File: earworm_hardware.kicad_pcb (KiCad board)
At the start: 2 copper layers, 37 parts, among them J1 Conn_01x02, J2 Conn_01x05, T1 LPR6235-752SMRC, U1 LTC3108EDE-TRPBF, U2 ADXL367BCCZ-RL7, U3 nRF54L15-QFXX, X1 32MHz

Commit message: Initial PCB Layout
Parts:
- removed the C11 at (83.0, 82.1)
- added C4: 10uF, Capacitor_SMD:C_0603_1608Metric, F.Cu at (93.6, 76.5)
- added X1: 32.768 kHz, earworm:Crystal_SMD_ECS_2012-2Pin_2.0x1.2mm, F.Cu at (94.1, 80.5)
- C1: renamed from C10; footprint Capacitor_SMD:C_0603_1608Metric -> Capacitor_SMD:C_0402_1005Metric
- C10: renamed from C7; footprint Capacitor_SMD:C_0603_1608Metric_Pad1.08x0.95mm_HandSolder -> Capacitor_SMD:C_0402_1005Metric; moved to B.Cu
- C11: renamed from C9; footprint Capacitor_SMD:C_0603_1608Metric -> Capacitor_SMD:C_0402_1005Metric; moved to B.Cu
- C12: renamed from C15; footprint Capacitor_SMD:C_0603_1608Metric -> Capacitor_SMD:C_0402_1005Metric
- C13: renamed from C8; footprint Capacitor_SMD:C_0603_1608Metric -> Capacitor_SMD:C_0402_1005Metric; moved to B.Cu
- C14: renamed from C16; footprint Capacitor_SMD:C_0603_1608Metric -> Capacitor_SMD:C_0402_1005Metric
- C15: renamed from C18; footprint Capacitor_SMD:C_0603_1608Metric -> Capacitor_SMD:C_0402_1005Metric
- C16: renamed from C19; footprint Capacitor_SMD:C_0603_1608Metric -> Capacitor_SMD:C_0402_1005Metric
- C17: renamed from C2; footprint Capacitor_SMD:C_0603_1608Metric -> Capacitor_SMD:C_0402_1005Metric
- C19: renamed from C5; moved to B.Cu
- C2: renamed from C12; footprint Capacitor_SMD:C_0603_1608Metric -> Capacitor_SMD:C_0402_1005Metric
- C20: renamed from C3; footprint Capacitor_SMD:C_0603_1608Metric -> Capacitor_SMD:C_0402_1005Metric
- C22: renamed from C4; footprint Capacitor_SMD:C_0603_1608Metric -> Capacitor_SMD:C_0402_1005Metric
- C3: renamed from C14; footprint Capacitor_SMD:C_0603_1608Metric -> Capacitor_SMD:C_0402_1005Metric
- C5: renamed from C13; footprint Capacitor_SMD:C_0603_1608Metric -> Capacitor_SMD:C_0402_1005Metric
- C6: renamed from C17; footprint Capacitor_SMD:C_0603_1608Metric -> Capacitor_SMD:C_0402_1005Metric
- FB1: footprint Inductor_SMD:L_0603_1608Metric -> Inductor_SMD:L_0402_1005Metric; moved to B.Cu
- FB2: footprint Inductor_SMD:L_0603_1608Metric -> Inductor_SMD:L_0402_1005Metric
- R1: renamed from R2; footprint Resistor_SMD:R_0603_1608Metric_Pad0.98x0.95mm_HandSolder -> Resistor_SMD:R_0402_1005Metric
- R2: renamed from R1; footprint Resistor_SMD:R_0603_1608Metric -> Resistor_SMD:R_0402_1005Metric; moved to B.Cu
- U2: moved to B.Cu
- moved C18 32.3 mm to (106.2, 87.5), turned to 180 degrees
- moved T1 30.0 mm to (105.0, 92.4), turned to -90 degrees
- moved C21 26.0 mm to (93.4, 86.9), turned to -90 degrees
- moved R1 21.9 mm to (103.9, 85.0)
- moved J2 21.8 mm to (107.7, 84.7), turned to -90 degrees
- moved U3 21.0 mm to (96.5, 92.7)
- moved C10 19.3 mm to (96.6, 75.7)
- moved C19 18.9 mm to (96.9, 87.2)
- moved C16 18.1 mm to (101.0, 75.6)
- moved C6 17.0 mm to (103.9, 84.0)
- moved L3 16.2 mm to (106.6, 80.7)
- moved C5 16.2 mm to (99.2, 86.7), turned to -90 degrees
- moved C15 16.1 mm to (101.0, 76.6)
- moved X2 15.7 mm to (104.8, 76.6), turned to -90 degrees
- moved C2 15.6 mm to (95.8, 75.6), turned to 90 degrees
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- renumbered C1 to C18, C6 to C21, C20 to C7, C21 to C8, C22 to C9, J2 to J1, J1 to J2, L2 to L1, L3 to L2, L4 to L3, L1 to L4, U3 to U1, U1 to U3, X1 to X2
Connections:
- U1 pad 1: unconnected-(U3-P1.00-Pad1) -> Net-(U1-P1.00)
- U1 pad 2: unconnected-(U3-P1.01-Pad2) -> Net-(U1-P1.01)
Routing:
- net Net-(U1-P2.05): track 0.00 -> 13.3 mm
- net Net-(U1-P2.02): track 0.00 -> 12.5 mm, vias 0 -> 1
- net Net-(U1-P2.01): track 0.00 -> 10.6 mm, vias 0 -> 1
- net Net-(U1-P2.04): track 0.00 -> 9.43 mm
- net Net-(T1-SB): track 0.00 -> 8.52 mm
- net Net-(U1-P2.03): track 0.00 -> 8.35 mm
- net Net-(J2-Pin_1): track 0.00 -> 5.71 mm
- net Net-(T1-AB): track 0.00 -> 5.36 mm
- net /Thermal Energy Harvesting Chain/VSTORE: track 0.00 -> 5.22 mm
- net Net-(U1-~{RESET}): track 0.00 -> 4.74 mm
- net Net-(U1-XC2): track 0.00 -> 4.47 mm
- net Net-(U1-XC1): track 0.00 -> 4.47 mm
- net Net-(U1-P1.01): track 0.00 -> 3.48 mm
- net GND: track 0.00 -> 3.30 mm
- net Net-(U1-DECD): track 0.00 -> 3.11 mm
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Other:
- board outline added: 17.3 x 22.2 mm
- board text added: "EECS 598 EARWORM"

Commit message: Initial RF layout
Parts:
- moved FB2 0.16 mm to (99.3, 74.6)
- moved L3 0.07 mm to (106.7, 80.8)
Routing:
- net Net-(U1-DECA): track 0.00 -> 9.02 mm, vias 0 -> 2
- net Net-(U2-VDDIO): track 0.00 -> 3.20 mm
- net Net-(U1-DECD): track 3.11 -> 5.85 mm
- net GND: track 3.30 -> 5.55 mm, vias 0 -> 1
- net VDD: track 2.39 -> 4.27 mm, vias 0 -> 1
- net Net-(U2-VREG_OUT): track 0.00 -> 1.43 mm
- added copper zone on B.Cu, net GND
- added copper zone on F.Cu, net Net-(U1-DECA)
- added copper zone on B.Cu, net Net-(U2-VS)

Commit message: DRC passed, everything done except RF
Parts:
- J1: footprint Connector_PinHeader_1.00mm:PinHeader_1x05_P1.00mm_Vertical -> Connector_PinHeader_2.54mm:PinHeader_1x05_P2.54mm_Vertical
- J2: footprint Connector_PinHeader_1.00mm:PinHeader_1x02_P1.00mm_Vertical -> Connector_PinHeader_2.54mm:PinHeader_1x02_P2.54mm_Vertical
- moved J1 6.94 mm to (93.6, 97.9), turned to 90 degrees
- moved J2 2.53 mm to (108.8, 87.0), turned to 180 degrees
- moved C18 2.00 mm to (105.9, 85.5), turned to 90 degrees
- moved C6 0.74 mm to (103.7, 84.7)
- moved R1 0.74 mm to (103.7, 85.7)
- moved C17 0.45 mm to (100.0, 92.7)
- moved C22 0.43 mm to (96.7, 89.8)
- moved C12 0.42 mm to (98.7, 76.6)
- moved C2 0.41 mm to (95.7, 76.0)
- moved C20 0.30 mm to (100.0, 91.7)
- moved T1 0.27 mm to (104.8, 92.4)
- moved L4 0.20 mm to (97.0, 75.6)
- moved C1 0.20 mm to (93.9, 82.7)
- moved C19 0.20 mm to (96.9, 87.4)
- moved C15 0.20 mm to (101.0, 76.4)
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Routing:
- net VDD: track 4.27 -> 47.7 mm, vias 1 -> 7
- net /nRF54L15 RFSoC/SWCLK: track 0.00 -> 19.2 mm, vias 0 -> 1
- net /nRF54L15 RFSoC/NRST: track 0.00 -> 16.6 mm, vias 0 -> 1
- net /nRF54L15 RFSoC/SWDIO: track 0.00 -> 16.6 mm, vias 0 -> 1
- net Net-(U1-DECA): track 9.02 -> 18.7 mm
- net GND: track 5.55 -> 14.6 mm, vias 1 -> 39
- net Net-(T1-SB): track 8.52 -> 0.00 mm
- net /Thermal Energy Harvesting Chain/VSTORE: track 5.22 -> 11.5 mm
- net Net-(J2-Pin_1): track 5.71 -> 1.70 mm
- net Net-(U3-VAUX): track 2.07 -> 5.98 mm, vias 0 -> 2
- net Net-(U1-P2.04): track 9.43 -> 13.1 mm, vias 0 -> 1
- net Net-(U1-P2.03): track 8.35 -> 11.2 mm, vias 0 -> 1
- net Net-(U1-P2.05): track 13.3 -> 16.1 mm, vias 0 -> 1
- net Net-(U1-P2.02): track 12.5 -> 11.8 mm
- net Net-(U1-DECD): track 5.85 -> 5.21 mm
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- added copper zone on F.Cu, net GND
- added copper zone on F.Cu, net Net-(J2-Pin_1)
- added copper zone on F.Cu, net Net-(T1-SB)
- added copper zone on F.Cu, net VDD
- removed copper zone on F.Cu, net Net-(U1-DECA)
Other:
- board size 17.3 x 22.2 mm -> 19.1 x 26.3 mm

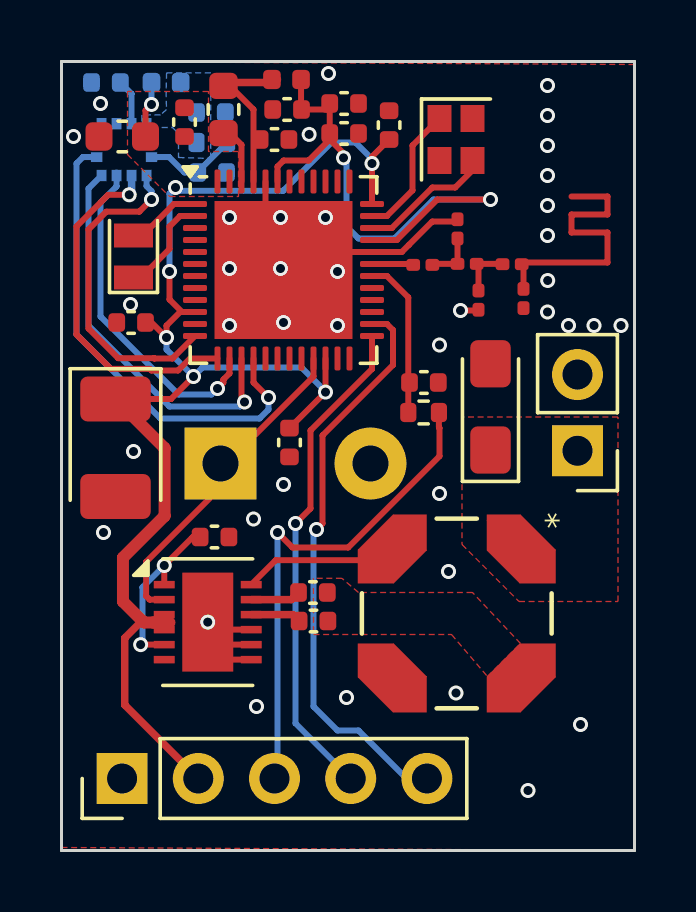
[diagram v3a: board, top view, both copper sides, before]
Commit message: 4 layer version, RF trace impedence matched
Missing SMA connector and a net tie for the other end of the inverted F
antenna to GND.
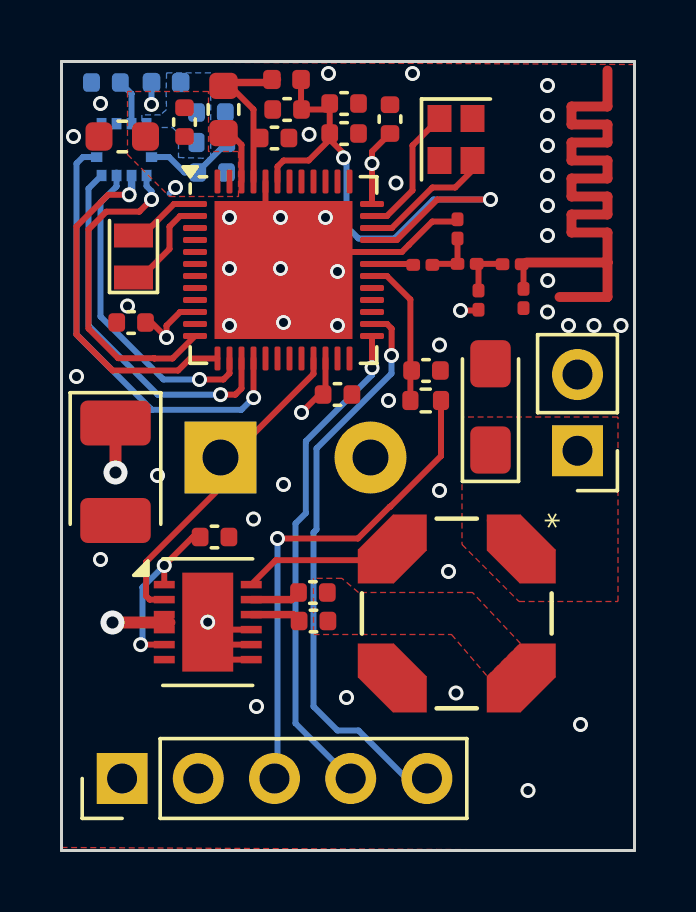
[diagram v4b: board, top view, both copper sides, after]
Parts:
- moved C5 2.26 mm to (100.8, 85.1), turned to 0 degrees
- moved C21 0.80 mm to (93.4, 87.7)
- moved C6 0.41 mm to (103.8, 84.3)
- moved R1 0.41 mm to (103.7, 85.3)
- moved C3 0.20 mm to (102.5, 75.9)
- moved C19 0.20 mm to (96.9, 87.2)
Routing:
- net VDD: track 47.7 -> 12.1 mm
- net Net-(U1-P2.05): track 16.1 -> 14.9 mm
- net Net-(U1-P2.04): track 13.1 -> 12.3 mm
- net GND: vias 39 -> 43
- added copper zone on In1.Cu, net GND
- added copper zone on In2.Cu, net VDD
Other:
- copper layers 2 -> 4

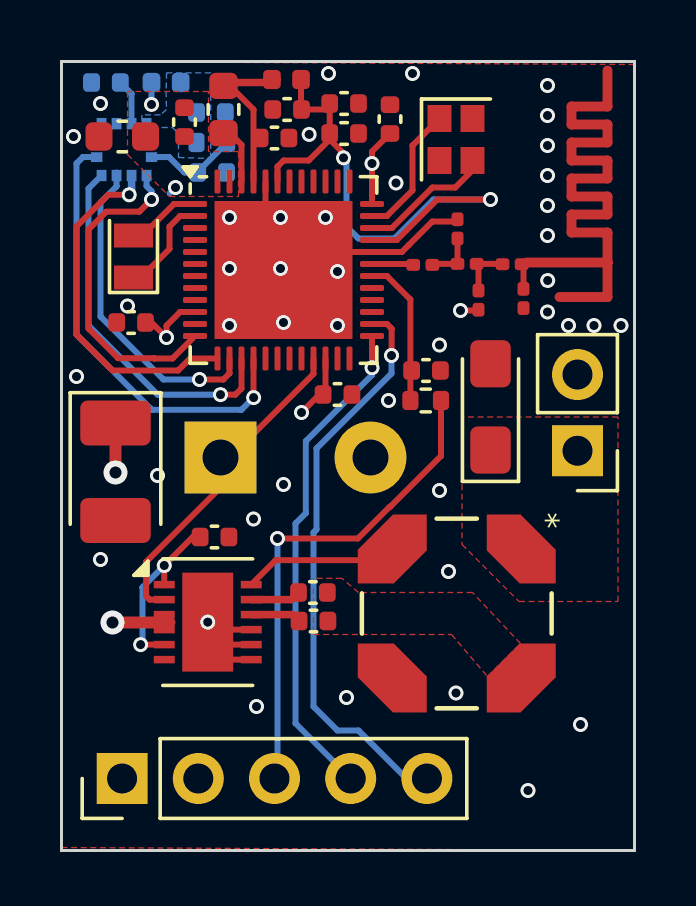
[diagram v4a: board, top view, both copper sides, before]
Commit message: Added the rest of the RF stuff
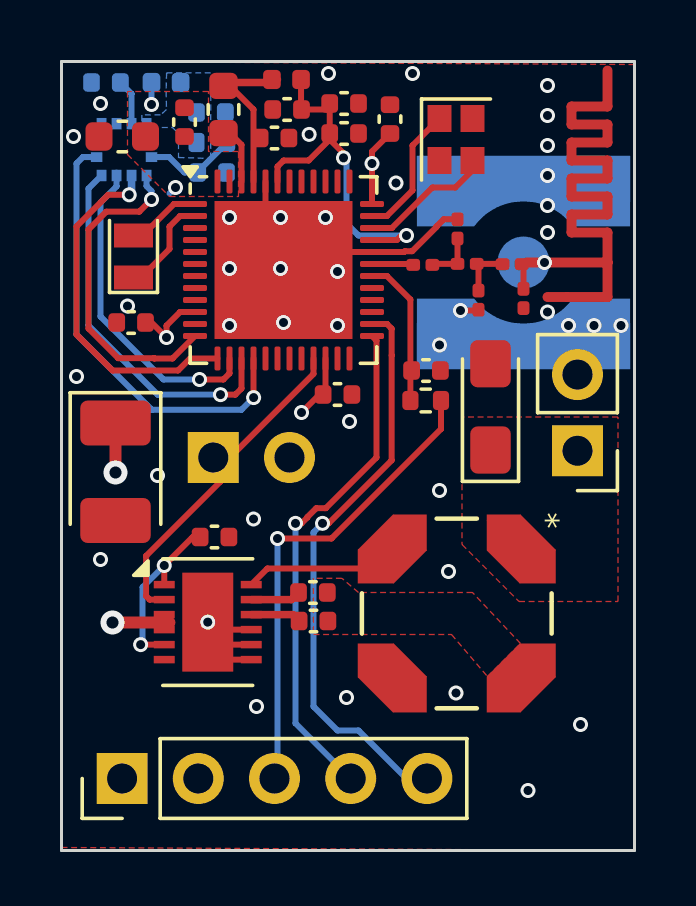
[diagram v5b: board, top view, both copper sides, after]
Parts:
- added NT1: NetTie_2, earworm:NetTie-2_SMD_Pad0.33mm, F.Cu at (108.1, 81.8)
- added REF**: SMA_Amphenol_132134-10_Vertical, Connector_Coaxial:SMA_Amphenol_132134-10_Vertical, B.Cu at (107.0, 80.7)
- C19: footprint earworm:CP_Radial_D13.5mm_P5.00mm -> Connector_PinHeader_2.54mm:PinHeader_1x02_P2.54mm_Vertical
- moved C19 0.24 mm to (96.7, 87.2), turned to -90 degrees
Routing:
- net Net-(U1-DECA): track 18.7 -> 12.0 mm
- net /nRF54L15 RFSoC/NRST: track 16.5 -> 16.0 mm
- net GND: vias 43 -> 41
- net /nRF54L15 RFSoC/RF: vias 0 -> 1

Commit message: changes from board review
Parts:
- added R3: 500k, Resistor_SMD:R_0402_1005Metric, F.Cu at (99.9, 91.6)
- added R4: 0, Resistor_SMD:R_0402_1005Metric, F.Cu at (93.3, 92.7)
- added R5: 0, Resistor_SMD:R_0402_1005Metric, B.Cu at (97.7, 94.7)
- added R6: 0, Resistor_SMD:R_0402_1005Metric, B.Cu at (97.7, 95.8)
- added R7: 0, Resistor_SMD:R_0402_1005Metric, B.Cu at (94.9, 94.7)
- added R8: 0, Resistor_SMD:R_0402_1005Metric, B.Cu at (94.9, 95.8)
- added TP1: TestPoint, TestPoint:TestPoint_Pad_D1.5mm, B.Cu at (95.8, 79.7)
- added TP2: TestPoint, TestPoint:TestPoint_Pad_D1.5mm, B.Cu at (98.9, 77.8)
- added TP3: TestPoint, TestPoint:TestPoint_Pad_D1.5mm, B.Cu at (97.0, 83.1)
- moved X1 1.28 mm to (93.2, 79.5)
- moved C17 0.93 mm to (100.0, 93.6)
- moved C20 0.87 mm to (100.0, 92.6)
- moved J1 0.70 mm to (93.6, 98.6)
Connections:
- U1 pad 14: Net-(U1-P2.03) -> unconnected-(U1-P2.03-Pad14)
- U1 pad 17: unconnected-(U1-P2.06-Pad17) -> Net-(U1-P2.06)
- U1 pad 4: unconnected-(U1-P1.03-Pad4) -> Net-(U1-P1.03)
- U1 pad 6: unconnected-(U1-P1.05-Pad6) -> Net-(U1-P1.05)
- U1 pad 8: unconnected-(U1-P1.07-Pad8) -> Net-(U1-P1.07)
- U2 pad 3: Net-(U1-P2.03) -> Net-(U1-P2.04)
- U2 pad 4: Net-(U1-P2.04) -> Net-(U1-P2.05)
- U2 pad 5: Net-(U1-P2.05) -> Net-(U1-P2.06)
- U3 pad 3: VDD -> Net-(U3-VOUT)
- U3 pad 4: VDD -> Net-(U3-VOUT)
- U3 pad 7: GND -> Net-(U3-VS2)
- U3 pad 8: GND -> Net-(U3-VS1)
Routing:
- net Net-(U1-P2.06): track 0.00 -> 15.7 mm, vias 0 -> 1
- net Net-(U1-P2.03): track 10.8 -> 0.00 mm, vias 1 -> 0
- net Net-(U3-VS1): track 0.00 -> 6.57 mm, vias 0 -> 1
- net Net-(U1-P1.05): track 0.00 -> 6.21 mm, vias 0 -> 1
- net Net-(U1-P2.01): track 11.0 -> 6.38 mm
- net Net-(U3-VS2): track 0.00 -> 4.14 mm, vias 0 -> 1
- net Net-(U1-P1.07): track 0.00 -> 3.85 mm, vias 0 -> 1
- net Net-(U3-VAUX): track 5.98 -> 8.41 mm
- net Net-(U1-P1.03): track 0.00 -> 2.15 mm, vias 0 -> 1
- net Net-(U1-P2.05): track 14.9 -> 12.9 mm
- net Net-(U1-P2.02): track 11.8 -> 9.90 mm
- net /nRF54L15 RFSoC/NRST: track 16.0 -> 17.7 mm
- net /nRF54L15 RFSoC/SWDIO: track 17.0 -> 18.7 mm
- net GND: track 14.6 -> 13.1 mm
- net VDD: track 12.1 -> 10.7 mm
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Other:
- board text added: "+"
- board text added: "-"
- board text added: "- + R D C"
- board text added: "1+"
- board text added: "1-"
- board text added: "2+"
- board text added: "2-"
- board text added: "Vo"

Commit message: rev0
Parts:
- removed REF**: SMA_Amphenol_132134-10_Vertical, Connector_Coaxial:SMA_Amphenol_132134-10_Vertical
- added J3: ~, Connector_Coaxial:SMA_Amphenol_132134-10_Vertical, B.Cu at (107.1, 79.8)
- C10: footprint Capacitor_SMD:C_0402_1005Metric -> Capacitor_SMD:C_0603_1608Metric
- moved C10 0.97 mm to (97.5, 75.5)
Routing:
- net GND: vias 41 -> 40
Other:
- board text added: "598 - EARWORM"
- board text removed: "EECS 598 EARWORM"

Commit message: various fixes
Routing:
- net /nRF54L15 RFSoC/NRST: track 17.7 -> 19.1 mm
- net /nRF54L15 RFSoC/SWCLK: track 19.3 -> 18.2 mm
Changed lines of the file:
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@@
 		)
 		(fp_text user "*"
-			(at -1.8415 0.75 -90)
-			(unlocked yes)
+			(at -1.8415 0.75 90)
 			(layer "B.SilkS")
 			(effects
@@
 		)
 		(fp_text user "*"
-			(at -1.8415 0.75 90)
+			(at -1.8415 0.75 -90)
+			(unlocked yes)
 			(layer "B.SilkS")
 			(effects
 				(font
-					(size 0.8 0.8)
+					(size 1 1)
 					(thickness 0.15)
 				)
@@
 		(fp_text user "*"
 			(at 0.1143 0.75 -90)
-			(unlocked yes)
 			(layer "B.Fab")
 			(effects
 				(font
-					(size 0.8 0.8)
+					(size 1 1)
 					(thickness 0.15)
 				)
@@
 		(pad "1" smd rect
 			(at -0.8636 0.750001)
-			(size 0.3302 0.381)
+			(size 0.3102 0.381)
 			(layers "B.Cu" "B.Paste" "B.Mask")
 			(net 40 "Net-(U1-P2.01)")
@@
 		(pad "2" smd rect
 			(at -0.8636 0.25)
-			(size 0.3302 0.381)
+			(size 0.3102 0.381)
 			(layers "B.Cu" "B.Paste" "B.Mask")
 			(net 51 "Net-(U1-P2.02)")
@@
 		(pad "3" smd rect
 			(at -0.8636 -0.25)
-			(size 0.3302 0.381)
+			(size 0.3102 0.381)
 			(layers "B.Cu" "B.Paste" "B.Mask")
 			(net 47 "Net-(U1-P2.04)")
@@
 		(pad "4" smd rect
 			(at -0.8636 -0.750001)
-			(size 0.3302 0.381)
+			(size 0.3102 0.381)
 			(layers "B.Cu" "B.Paste" "B.Mask")
 			(net 37 "Net-(U1-P2.05)")
@@
 		(pad "5" smd rect
 			(at -0.25 -0.9144 90)
-			(size 0.3302 0.381)
+			(size 0.31 0.381)
 			(layers "B.Cu" "B.Paste" "B.Mask")
 			(net 35 "Net-(U1-P2.06)")
@@
 		(pad "6" smd rect
 			(at 0.25 -0.9144 90)
-			(size 0.3302 0.381)
+			(size 0.3102 0.381)
 			(layers "B.Cu" "B.Paste" "B.Mask")
 			(net 27 "unconnected-(U2-INT2-Pad6)")
@@
 		(pad "7" smd rect
 			(at 0.8636 -0.750001)
-			(size 0.3302 0.381)
+			(size 0.3102 0.381)
 			(layers "B.Cu" "B.Paste" "B.Mask")
 			(net 2 "GND")
@@
 		(pad "8" smd rect
 			(at 0.8636 -0.25)
-			(size 0.3302 0.381)
+			(size 0.3102 0.381)
 			(layers "B.Cu" "B.Paste" "B.Mask")
 			(net 2 "GND")
@@
 		(pad "9" smd rect
 			(at 0.8636 0.25)
-			(size 0.3302 0.381)
+			(size 0.3102 0.381)
 			(layers "B.Cu" "B.Paste" "B.Mask")
 			(net 10 "Net-(U2-VREG_OUT)")
@@
 		(pad "10" smd rect
 			(at 0.8636 0.750001)
-			(size 0.3302 0.381)
+			(size 0.3102 0.381)
 			(layers "B.Cu" "B.Paste" "B.Mask")
 			(net 9 "Net-(U2-VS)")
@@
 		(pad "11" smd rect
 			(at 0.25 0.9144 90)
-			(size 0.3302 0.381)
+			(size 0.3102 0.381)
 			(layers "B.Cu" "B.Paste" "B.Mask")
 			(net 2 "GND")
@@
 		(pad "12" smd rect
 			(at -0.25 0.9144 90)
-			(size 0.3302 0.381)
+			(size 0.3102 0.381)
 			(layers "B.Cu" "B.Paste" "B.Mask")
 			(net 11 "Net-(U2-VDDIO)")
@@
 	)
 	(segment
-		(start 102.4 97.38)
-		(end 101.18 98.6)
+		(start 99.4 89.395)
+		(end 102.3 92.295)
 		(width 0.2)
 		(layer "B.Cu")
@@
 	)
 	(segment
-		(start 102.4 92.395)
-		(end 102.4 97.38)
+		(start 102.3 97.48)
+		(end 101.18 98.6)
 		(width 0.2)
 		(layer "B.Cu")
@@
 	)
 	(segment
-		(start 99.4 89.395)
-		(end 102.4 92.395)
+		(start 102.3 92.295)
+		(end 102.3 97.48)
 		(width 0.2)
 		(layer "B.Cu")
@@
 	)
 	(segment
-		(start 100.1 91.2)
-		(end 100.1 97.14)
+		(start 101.7 95.54)
+		(end 98.7 98.54)
 		(width 0.2)
 		(layer "B.Cu")
@@
 	)
 	(segment
-		(start 98.8 89.9)
-		(end 100.1 91.2)
+		(start 98.9 89.9)
+		(end 101.7 92.7)
 		(width 0.2)
 		(layer "B.Cu")
@@
 	)
 	(segment
-		(start 100.1 97.14)
-		(end 98.7 98.54)
+		(start 101.7 92.7)
+		(end 101.7 95.54)
+		(width 0.2)
+		(layer "B.Cu")
+		(net 19)
+	)
+	(segment
+		(start 98.8 89.9)
+		(end 98.9 89.9)
 		(width 0.2)
 		(layer "B.Cu")
@@
 	)
 	(segment
-		(start 103.78 91.08)
+		(start 102.9 97.02)
 		(end 103.78 97.9)
 		(width 0.2)
@@
 	)
 	(segment
-		(start 102.095 89.395)
-		(end 103.78 91.08)
+		(start 102.9 92.1)
+		(end 102.9 97.02)
+		(width 0.2)
+		(layer "B.Cu")
+		(net 20)
+	)
+	(segment
+		(start 100.300003 89.500003)
+		(end 102.9 92.1)
 		(width 0.2)
 		(layer "B.Cu")
@@
 	(segment
 		(start 100.300003 89.395)
-		(end 102.095 89.395)
+		(end 100.300003 89.500003)
 		(width 0.2)
 		(layer "B.Cu")
@@
 	)
 	(segment
-		(start 97.34 84.76)
-		(end 95.15 84.76)
+		(start 95 84.6)
+		(end 92.9 82.5)
 		(width 0.2)
 		(layer "B.Cu")
@@
 	)
 	(segment
-		(start 93.4356 78.1644)
-		(end 93.4356 77.7)
+		(start 97.34 84.76)
+		(end 95.15 84.76)
 		(width 0.2)
 		(layer "B.Cu")
@@
 	)
 	(segment
-		(start 92.9 78.7)
-		(end 93.4356 78.1644)
+		(start 95.15 84.76)
+		(end 94.99 84.6)
 		(width 0.2)
 		(layer "B.Cu")
@@
 	)
 	(segment
-		(start 95.15 84.76)
-		(end 94.99 84.6)
+		(start 92.9 78.7)
+		(end 93.4356 78.1644)
 		(width 0.2)
 		(layer "B.Cu")
@@
 	)
 	(segment
-		(start 95 84.6)
-		(end 92.9 82.5)
+		(start 97.4 84.7)
+		(end 97.34 84.76)
 		(width 0.2)
 		(layer "B.Cu")
@@
 	)
 	(segment
-		(start 97.4 84.7)
-		(end 97.34 84.76)
+		(start 93.4356 78.1644)
+		(end 93.4356 77.8)
 		(width 0.2)
 		(layer "B.Cu")
@@
 	)
 	(segment
-		(start 96.295 80.705)
-		(end 98.9 78.1)
-		(width 0.2)
-		(layer "B.Cu")
-		(net 59)
-	)
-	(segment
-		(start 95.035601 80.705)
-		(end 96.295 80.705)
+		(start 94.940601 80.8)
+		(end 96.2 80.8)
 		(width 0.2)
 		(layer "B.Cu")
@@
 	)
 	(segment
-		(start 94.940601 80.8)
-		(end 95.035601 80.705)
+		(start 96.2 80.8)
+		(end 98.9 78.1)
 		(width 0.2)
 		(layer "B.Cu")
